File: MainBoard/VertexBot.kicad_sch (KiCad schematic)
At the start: 48 parts, among them J1 Conn_01x02, J4 Left Motor, J5 Right Motor, J6 Led Strip, J7 Speaker, Q1 BSS138, Q2 BSS138, Q3 BSS138, SW1 SW_SPST, U1 DRV8830DGQR, U10 MAX4466, U11 MAX4466, U12 ESP32-S3-CAM-B, U13 ESP32-S3-CAM-A, U2 DRV8830DGQR, U3 S13V30F5, U4 MAX98357A, U5 INMP441, U6 0.96 INCH OLED, U7 DRV5033AJxLPG, U8 DRV5033AJxLPG, U9 MPU 6050

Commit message: Add footprints for SMD passive components Link to public software repository
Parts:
- C1, C2, C3: footprint (none) -> Capacitor_SMD:C_0201_0603Metric
- D1, D2: footprint (none) -> LED_SMD:LED_0201_0603Metric
- J1: footprint (none) -> Connector_JST:JST_XH_B3B-XH-A_1x03_P2.50mm_Vertical
- R1, R10, R11, R12, R13, R14, R15, R2, R3, R4, R5, R6, R7, R8, R9: footprint (none) -> Resistor_SMD:R_0201_0603Metric
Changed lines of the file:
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@@
 			)
 		)
-		(property "Footprint" ""
+		(property "Footprint" "LED_SMD:LED_0201_0603Metric"
 			(at 105.41 55.88 0)
 			(effects
@@
 			)
 		)
-		(property "Footprint" ""
+		(property "Footprint" "Capacitor_SMD:C_0201_0603Metric"
 			(at 205.4352 55.88 0)
 			(effects
@@
 			)
 		)
-		(property "Footprint" ""
+		(property "Footprint" "Resistor_SMD:R_0201_0603Metric"
 			(at 158.242 64.77 90)
 			(effects
@@
 			)
 		)
-		(property "Footprint" ""
+		(property "Footprint" "Resistor_SMD:R_0201_0603Metric"
 			(at 103.632 63.5 90)
 			(effects
@@
 			)
 		)
-		(property "Footprint" ""
+		(property "Footprint" "Resistor_SMD:R_0201_0603Metric"
 			(at 165.862 96.52 90)
 			(effects
@@
 			)
 		)
-		(property "Footprint" ""
+		(property "Footprint" "Resistor_SMD:R_0201_0603Metric"
 			(at 109.982 129.54 90)
 			(effects
@@
 			)
 		)
-		(property "Footprint" ""
+		(property "Footprint" "Connector_JST:JST_XH_B3B-XH-A_1x03_P2.50mm_Vertical"
 			(at 31.75 87.63 0)
 			(effects
@@
 			)
 		)
-		(property "Footprint" ""
+		(property "Footprint" "Resistor_SMD:R_0201_0603Metric"
 			(at 64.77 40.132 90)
 			(effects
@@
 			)
 		)
-		(property "Footprint" ""
+		(property "Footprint" "Resistor_SMD:R_0201_0603Metric"
 			(at 116.332 119.38 90)
 			(effects
@@
 			)
 		)
-		(property "Footprint" ""
+		(property "Footprint" "Capacitor_SMD:C_0201_0603Metric"
 			(at 69.5452 54.61 0)
 			(effects
@@
 			)
 		)
-		(property "Footprint" ""
+		(property "Footprint" "Capacitor_SMD:C_0201_0603Metric"
 			(at 238.4552 53.34 0)
 			(effects
@@
 			)
 		)
-		(property "Footprint" ""
+		(property "Footprint" "Resistor_SMD:R_0201_0603Metric"
 			(at 130.302 129.54 90)
 			(effects
@@
 			)
 		)
-		(property "Footprint" ""
+		(property "Footprint" "Resistor_SMD:R_0201_0603Metric"
 			(at 224.282 43.18 90)
 			(effects
@@
 			)
 		)
-		(property "Footprint" ""
+		(property "Footprint" "Resistor_SMD:R_0201_0603Metric"
 			(at 137.922 119.38 90)
 			(effects
@@
 			)
 		)
-		(property "Footprint" ""
+		(property "Footprint" "Resistor_SMD:R_0201_0603Metric"
 			(at 98.552 74.93 90)
 			(effects
@@
 			)
 		)
-		(property "Footprint" ""
+		(property "Footprint" "Resistor_SMD:R_0201_0603Metric"
 			(at 151.892 129.54 90)
 			(effects
@@
 			)
 		)
-		(property "Footprint" ""
+		(property "Footprint" "Resistor_SMD:R_0201_0603Metric"
 			(at 115.062 45.72 90)
 			(effects
@@
 			)
 		)
-		(property "Footprint" ""
+		(property "Footprint" "Resistor_SMD:R_0201_0603Metric"
 			(at 96.012 118.11 90)
 			(effects
@@
 			)
 		)
-		(property "Footprint" ""
+		(property "Footprint" "Resistor_SMD:R_0201_0603Metric"
 			(at 98.552 85.09 90)
 			(effects
@@
 			)
 		)
-		(property "Footprint" ""
+		(property "Footprint" "LED_SMD:LED_0201_0603Metric"
 			(at 160.02 55.88 0)
 			(effects
@@
 			)
 		)
-		(property "Footprint" ""
+		(property "Footprint" "Resistor_SMD:R_0201_0603Metric"
 			(at 258.572 43.18 90)
 			(effects

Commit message: Add INMP441 module footprint
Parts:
- U5: footprint (none) -> Vertex_Bot:INMP441
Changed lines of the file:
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@@
 			)
 		)
-		(property "Footprint" ""
+		(property "Footprint" "Vertex_Bot:INMP441"
 			(at 223.52 80.01 0)
 			(effects

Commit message: Footprint for OLED, INMP441, Test Points Fix Library broken dependency
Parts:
- TP1, TP2, TP3, TP4: footprint (none) -> TestPoint:TestPoint_Pad_3.0x3.0mm
- U6: footprint (none) -> Vertex_Bot:OLED_0_96_INCH
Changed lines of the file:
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@@
 			)
 		)
-		(property "Footprint" ""
+		(property "Footprint" "TestPoint:TestPoint_Pad_3.0x3.0mm"
 			(at 92.71 113.03 0)
 			(effects
@@
 			)
 		)
-		(property "Footprint" ""
+		(property "Footprint" "TestPoint:TestPoint_Pad_3.0x3.0mm"
 			(at 231.14 54.61 0)
 			(effects
@@
 			)
 		)
-		(property "Footprint" ""
+		(property "Footprint" "TestPoint:TestPoint_Pad_3.0x3.0mm"
 			(at 64.77 93.98 0)
 			(effects
@@
 			)
 		)
-		(property "Footprint" ""
+		(property "Footprint" "Vertex_Bot:OLED_0_96_INCH"
 			(at 186.69 41.91 0)
 			(effects
@@
 			)
 		)
-		(property "Footprint" ""
+		(property "Footprint" "TestPoint:TestPoint_Pad_3.0x3.0mm"
 			(at 265.43 52.07 0)
 			(effects

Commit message: Library cleanup
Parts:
- D1, D2: footprint LED_SMD:LED_0201_0603Metric -> LED_SMD:LED_0805_2012Metric
- F1: footprint footprints:FUSE_0031.8211_SCH -> Vertex_Bot:FUSE_0031.8211_SCH
- SW1: footprint KiCad:S101031MS02Q -> Vertex_Bot:S101031MS02Q
- U1, U2: footprint footprints:DGQ10_2P18X1P72 -> Vertex_Bot:DGQ10_2P18X1P72
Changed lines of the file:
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@@
 			)
 		)
-		(property "Footprint" "LED_SMD:LED_0201_0603Metric"
+		(property "Footprint" "LED_SMD:LED_0805_2012Metric"
 			(at 105.41 55.88 0)
 			(effects
@@
 			)
 		)
-		(property "Footprint" "footprints:DGQ10_2P18X1P72"
+		(property "Footprint" "Vertex_Bot:DGQ10_2P18X1P72"
 			(at 72.39 39.37 0)
 			(effects
@@
 			)
 		)
-		(property "Footprint" "footprints:DGQ10_2P18X1P72"
+		(property "Footprint" "Vertex_Bot:DGQ10_2P18X1P72"
 			(at 129.54 39.37 0)
 			(effects
@@
 			)
 		)
-		(property "Footprint" "LED_SMD:LED_0201_0603Metric"
+		(property "Footprint" "LED_SMD:LED_0805_2012Metric"
 			(at 160.02 55.88 0)
 			(effects
@@
 			)
 		)
-		(property "Footprint" "footprints:FUSE_0031.8211_SCH"
+		(property "Footprint" "Vertex_Bot:FUSE_0031.8211_SCH"
 			(at 72.39 90.17 0)
 			(effects
@@
 			)
 		)
-		(property "Footprint" "KiCad:S101031MS02Q"
+		(property "Footprint" "Vertex_Bot:S101031MS02Q"
 			(at 64.77 90.17 0)
 			(effects

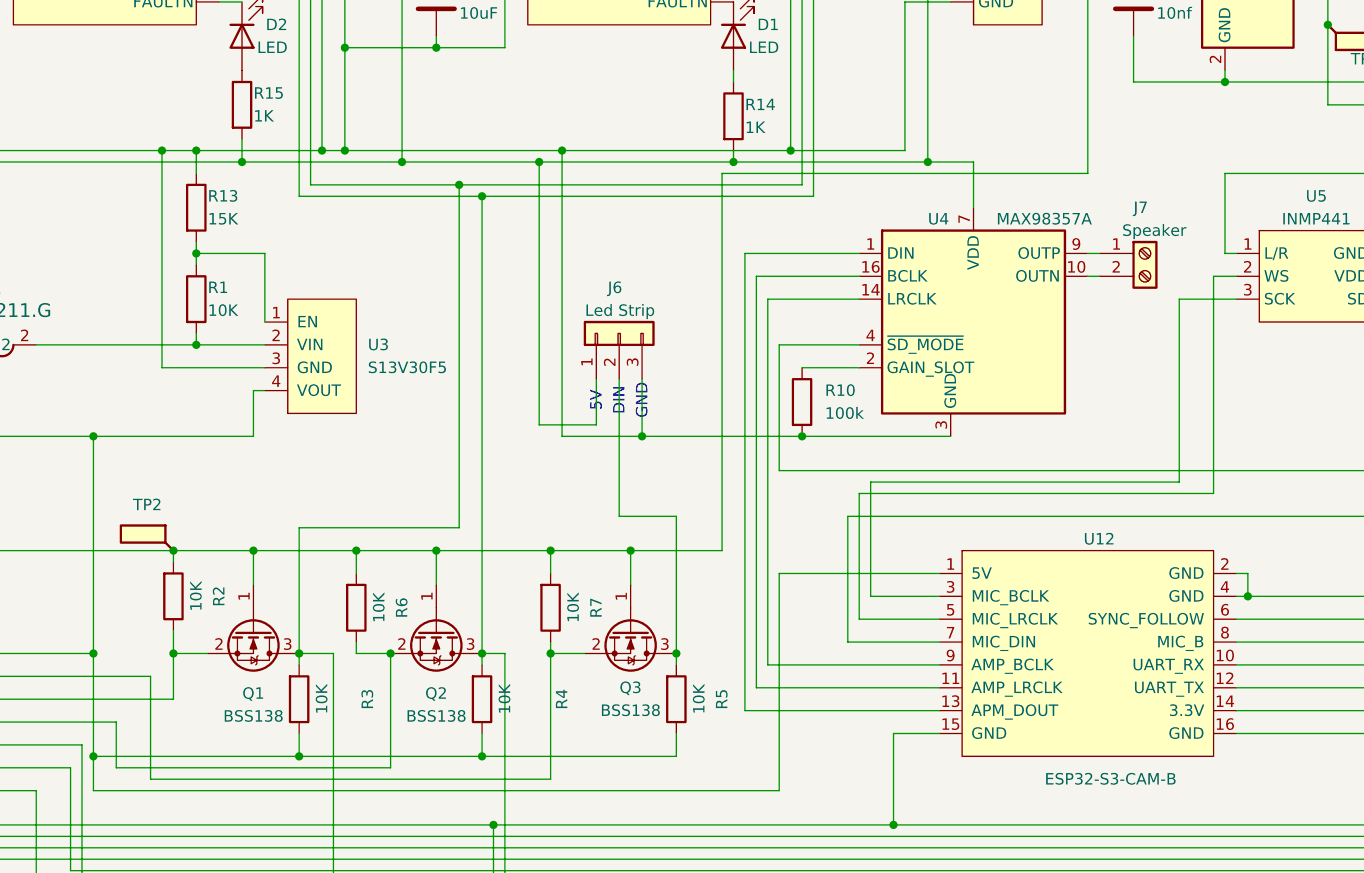
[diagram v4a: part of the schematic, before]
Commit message: Add MAX98357 and S13V30F5 footprints
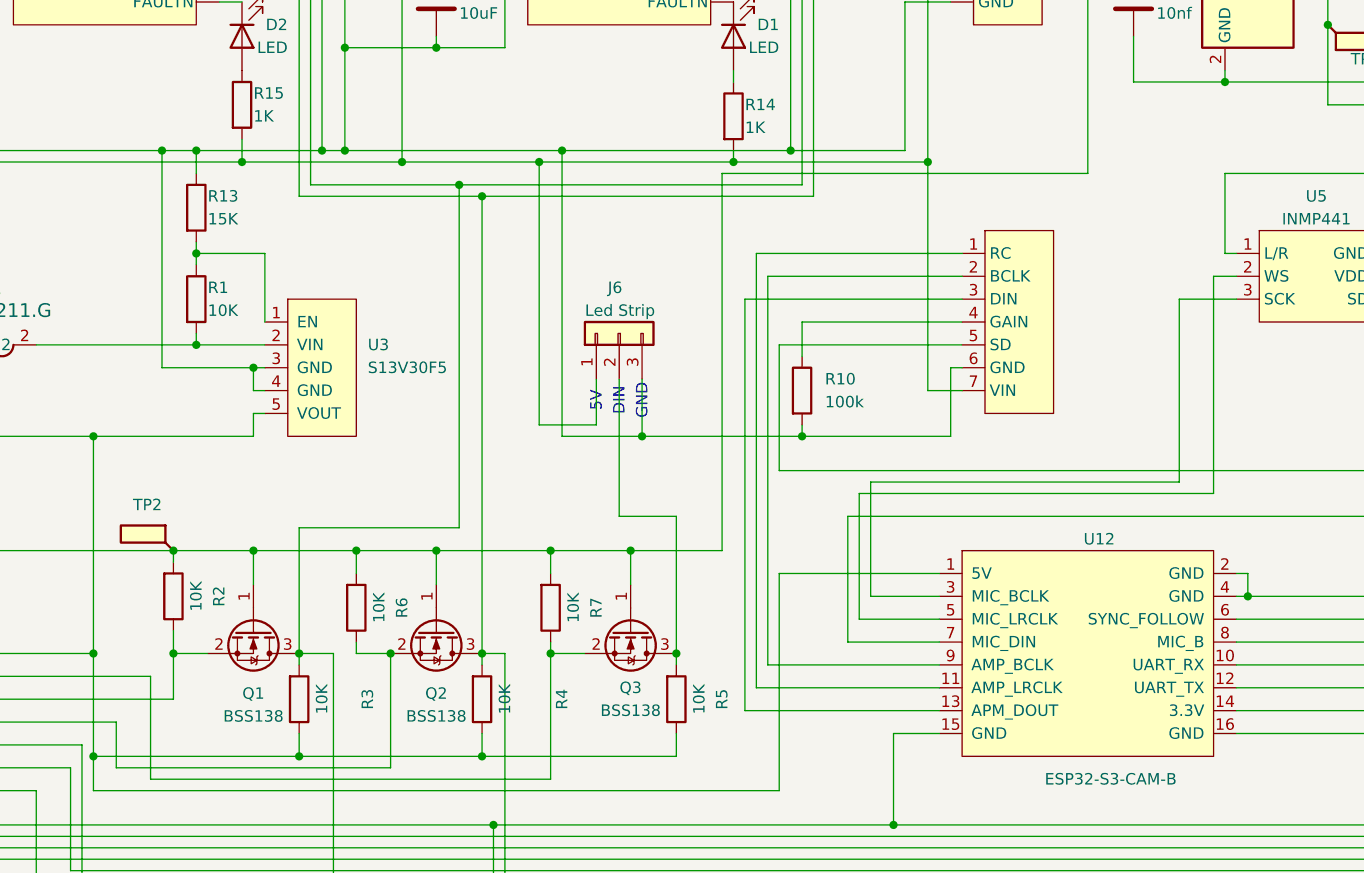
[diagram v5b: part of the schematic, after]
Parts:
- removed J7: Speaker, symbol Connector:Screw_Terminal_01x02
- removed U4: MAX98357A, Package_DFN_QFN:TQFN-16-1EP_3x3mm_P0.5mm_EP1.23x1.23mm, symbol VertexBot:MAX98357A
- added U14: MAX98357A, Vertex_Bot:MAX98357, symbol VertexBot:MAX98357A
- U12: footprint (none) -> Connector_PinSocket_2.54mm:PinSocket_2x08_P2.54mm_Vertical
- U13: footprint (none) -> Connector_PinSocket_2.54mm:PinSocket_2x07_P2.54mm_Vertical
- U3: footprint (none) -> Vertex_Bot:S13V30F5
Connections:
- net +5V: now also U3.5 (VOUT), U14.7 (VIN); no longer U3.4 (VOUT)
- net GND: now also U3.4 (GND), U14.6 (GND)
- net at R10.1: now also U14.4 (GAIN)
- net at U12.13 (APM_DOUT): now also U14.3 (DIN)
- net at U12.9 (AMP_BCLK): now also U14.2 (BCLK)
- net at U12.11 (AMP_LRCLK): now also U14.1 (RC)
- net at U12.14 (3.3V), U5.1 (L/R), U5.5 (VDD): now also U14.5 (SD)
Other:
- moved on the sheet: R10

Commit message: Footprints complete and rough test placement on the board
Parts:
- C4: footprint (none) -> Capacitor_SMD:C_0201_0603Metric
- J1: value Conn_01x02 -> Battery; footprint Connector_JST:JST_XH_B3B-XH-A_1x03_P2.50mm_Vertical -> Connector_JST:JST_XH_S3B-XH-A-1_1x02_P2.50mm_Horizontal; symbol Connector_Generic:Conn_01x03 -> Connector_Generic:Conn_01x02
- J4, J5: footprint (none) -> Connector_JST:JST_PH_S2B-PH-K_1x02_P2.00mm_Horizontal
- J6: footprint Connector_JST:JST_XH_B3B-XH-A_1x03_P2.50mm_Vertical -> Connector_JST:JST_XH_S3B-XH-A-1_1x03_P2.50mm_Horizontal
- SW1: footprint Vertex_Bot:S101031MS02Q -> Vertex_Bot:L101011MS02Q
- U10, U11: footprint (none) -> Connector_PinSocket_2.54mm:PinSocket_1x03_P2.54mm_Vertical
- U12: footprint Connector_PinSocket_2.54mm:PinSocket_2x08_P2.54mm_Vertical -> Vertex_Bot:CAM_B_BOARD_VERTICAL
- U13: footprint Connector_PinSocket_2.54mm:PinSocket_2x07_P2.54mm_Vertical -> Vertex_Bot:CAM_A_BOARD_VERTICAL
- U3: footprint Vertex_Bot:S13V30F5 -> Vertex_Bot:S13V30F5_VERTICAL
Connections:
- net GND: now also J1.2 (Pin_2), SW1.1 (A), TP1.1
- no-connect marks 6 -> 5
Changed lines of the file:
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@@
 	(text "GND"
 		(exclude_from_sim no)
-		(at 27.94 85.09 0)
+		(at 27.94 87.63 0)
 		(effects
 			(font
@@
 	)
 	(junction
+		(at 39.37 90.17)
+		(diameter 0)
+		(color 0 0 0 0)
+	)
+	(junction
 		(at 116.84 68.58)
 		(diameter 0)
@@
 	)
 	(junction
-		(at 39.37 85.09)
+		(at 39.37 87.63)
 		(diameter 0)
 		(color 0 0 255 1)
@@
 	)
 	(no_connect
-		(at 36.83 87.63)
-	)
-	(no_connect
 		(at 102.87 49.53)
 	)
@@
 	(wire
 		(pts
+			(xy 39.37 90.17) (xy 59.69 90.17)
+		)
+		(stroke
+			(width 0)
+			(type default)
+		)
+	)
+	(wire
+		(pts
 			(xy 165.1 115.57) (xy 165.1 139.7)
 		)
@@
 	(wire
 		(pts
-			(xy 36.83 85.09) (xy 39.37 85.09)
+			(xy 36.83 87.63) (xy 39.37 87.63)
 		)
 		(stroke
@@
 	(wire
 		(pts
+			(xy 39.37 90.17) (xy 39.37 124.46)
+		)
+		(stroke
+			(width 0)
+			(type default)
+			(color 0 0 255 1)
+		)
+	)
+	(wire
+		(pts
 			(xy 111.76 110.49) (xy 111.76 124.46)
 		)
@@
 	(wire
 		(pts
-			(xy 39.37 85.09) (xy 39.37 124.46)
+			(xy 39.37 87.63) (xy 39.37 90.17)
 		)
 		(stroke
@@
 	(wire
 		(pts
-			(xy 39.37 68.58) (xy 39.37 85.09)
+			(xy 39.37 68.58) (xy 39.37 87.63)
 		)
 		(stroke
@@
 	(wire
 		(pts
-			(xy 36.83 90.17) (xy 59.69 90.17)
+			(xy 36.83 90.17) (xy 39.37 90.17)
 		)
 		(stroke
@@
 			)
 		)
-		(property "Footprint" ""
+		(property "Footprint" "Connector_PinSocket_2.54mm:PinSocket_1x03_P2.54mm_Vertical"
 			(at 110.49 163.83 0)
 			(effects
@@
 	)
 	(symbol
-		(lib_id "Connector_Generic:Conn_01x03")
+		(lib_id "Connector_Generic:Conn_01x02")
 		(at 31.75 87.63 0)
 		(mirror y)
@@
 			)
 		)
-		(property "Value" "Conn_01x02"
+		(property "Value" "Battery"
 			(at 34.29 83.82 0)
 			(effects
@@
 			)
 		)
-		(property "Footprint" "Connector_JST:JST_XH_B3B-XH-A_1x03_P2.50mm_Vertical"
+		(property "Footprint" "Connector_JST:JST_XH_S3B-XH-A-1_1x02_P2.50mm_Horizontal"
 			(at 31.75 87.63 0)
 			(effects
@@
 			)
 		)
-		(property "Description" "Generic connector, single row, 01x03, script generated (kicad-library-utils/schlib/autogen/connector/)"
+		(property "Description" "Generic connector, single row, 01x02, script generated (kicad-library-utils/schlib/autogen/connector/)"
 			(at 31.75 87.63 0)
 			(effects
@@
 		(pin "2"
 		)
-		(pin "3"
-		)
 		(instances
 			(project ""
@@
 			)
 		)
-		(property "Footprint" ""
+		(property "Footprint" "Connector_JST:JST_PH_S2B-PH-K_1x02_P2.00mm_Horizontal"
 			(at 127 29.21 0)
 			(effects
@@
 			)
 		)
-		(property "Footprint" "Connector_JST:JST_XH_B3B-XH-A_1x03_P2.50mm_Vertical"
+		(property "Footprint" "Connector_JST:JST_XH_S3B-XH-A-1_1x03_P2.50mm_Horizontal"
 			(at 147.32 88.9 0)
 			(effects
@@
 			)
 		)
-		(property "Footprint" ""
+		(property "Footprint" "Capacitor_SMD:C_0201_0603Metric"
 			(at 127.9652 55.88 0)
 			(effects
@@
 			)
 		)
-		(property "Footprint" "Connector_PinSocket_2.54mm:PinSocket_2x08_P2.54mm_Vertical"
+		(property "Footprint" "Vertex_Bot:CAM_B_BOARD_VERTICAL"
 			(at 190.5 123.19 0)
 			(effects
@@
 			)
 		)
-		(property "Footprint" ""
+		(property "Footprint" "Connector_JST:JST_PH_S2B-PH-K_1x02_P2.00mm_Horizontal"
 			(at 72.39 29.21 0)
 			(effects
@@
 			)
 		)
-		(property "Footprint" "Vertex_Bot:S13V30F5"
+		(property "Footprint" "Vertex_Bot:S13V30F5_VERTICAL"
 			(at 113.03 92.71 0)
 			(effects
@@
 			)
 		)
-		(property "Footprint" "Connector_PinSocket_2.54mm:PinSocket_2x07_P2.54mm_Vertical"
+		(property "Footprint" "Vertex_Bot:CAM_A_BOARD_VERTICAL"
 			(at 74.93 132.08 0)
 			(effects
@@
 			)
 		)
-		(property "Footprint" ""
+		(property "Footprint" "Connector_PinSocket_2.54mm:PinSocket_1x03_P2.54mm_Vertical"
 			(at 139.7 163.83 0)
 			(effects
@@
 			)
 		)
-		(property "Footprint" "Vertex_Bot:S101031MS02Q"
+		(property "Footprint" "Vertex_Bot:L101011MS02Q"
 			(at 64.77 90.17 0)
 			(effects
@@
 			)
 		)
-		(property "Datasheet" "https://au.element14.com/c-k-components/s101031ms02q/slide-switch-spst-6a-250v-tht/dp/2931779"
+		(property "Datasheet" "https://au.mouser.com/en/ProductDetail/CK/L101011MS02Q?qs=LgMIjt8LuD9j8DCrk%2FIjYQ%3D%3D"
 			(at 64.77 90.17 0)
 			(effects

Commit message: Fix for correct battery connector footprint
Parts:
- J1: footprint Connector_JST:JST_XH_S3B-XH-A-1_1x02_P2.50mm_Horizontal -> Connector_JST:JST_XH_S2B-XH-A-1_1x02_P2.50mm_Horizontal
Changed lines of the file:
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@@
 			)
 		)
-		(property "Footprint" "Connector_JST:JST_XH_S3B-XH-A-1_1x02_P2.50mm_Horizontal"
+		(property "Footprint" "Connector_JST:JST_XH_S2B-XH-A-1_1x02_P2.50mm_Horizontal"
 			(at 31.75 87.63 0)
 			(effects

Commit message: Adjust divider values for cutoff at 3V (en = 1V) Add Tolerance (0.1%)
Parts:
- R1: value 10K -> 20K 0.1%
- R13: value 15K -> 10K 0.1%
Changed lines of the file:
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@@
 			)
 		)
-		(property "Value" "15K"
+		(property "Value" "10K 0.1%"
 			(at 101.6 76.2 0)
 			(effects
@@
 			)
 		)
-		(property "Value" "10K"
-			(at 101.6 86.36 0)
-			(effects
-				(font
+		(property "Value" "20K 0.1%"
+			(at 96.52 88.9 0)
+			(effects
+				(font
